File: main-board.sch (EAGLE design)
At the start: 53 parts, among them IC1 MEGA328-PB, IC2 MCP73831, IC3 LE33, Q1 3,6864 MHz, Q4 TSM2302CX, T1 IRF7306

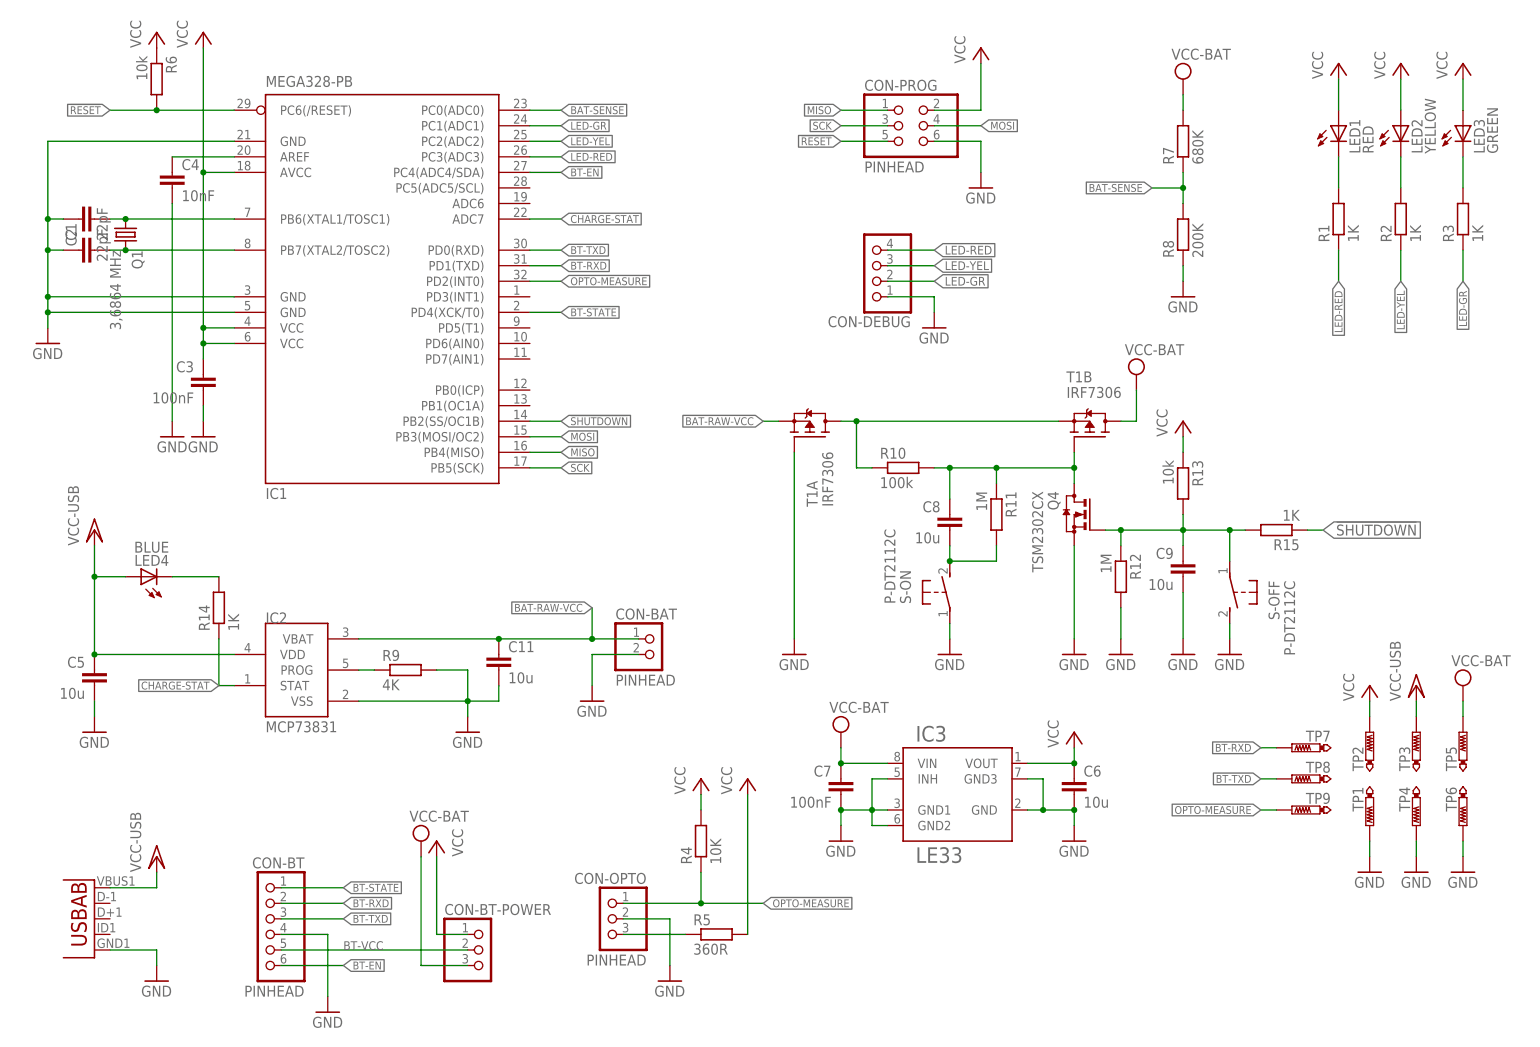
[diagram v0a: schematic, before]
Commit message: Optimize for BOM.
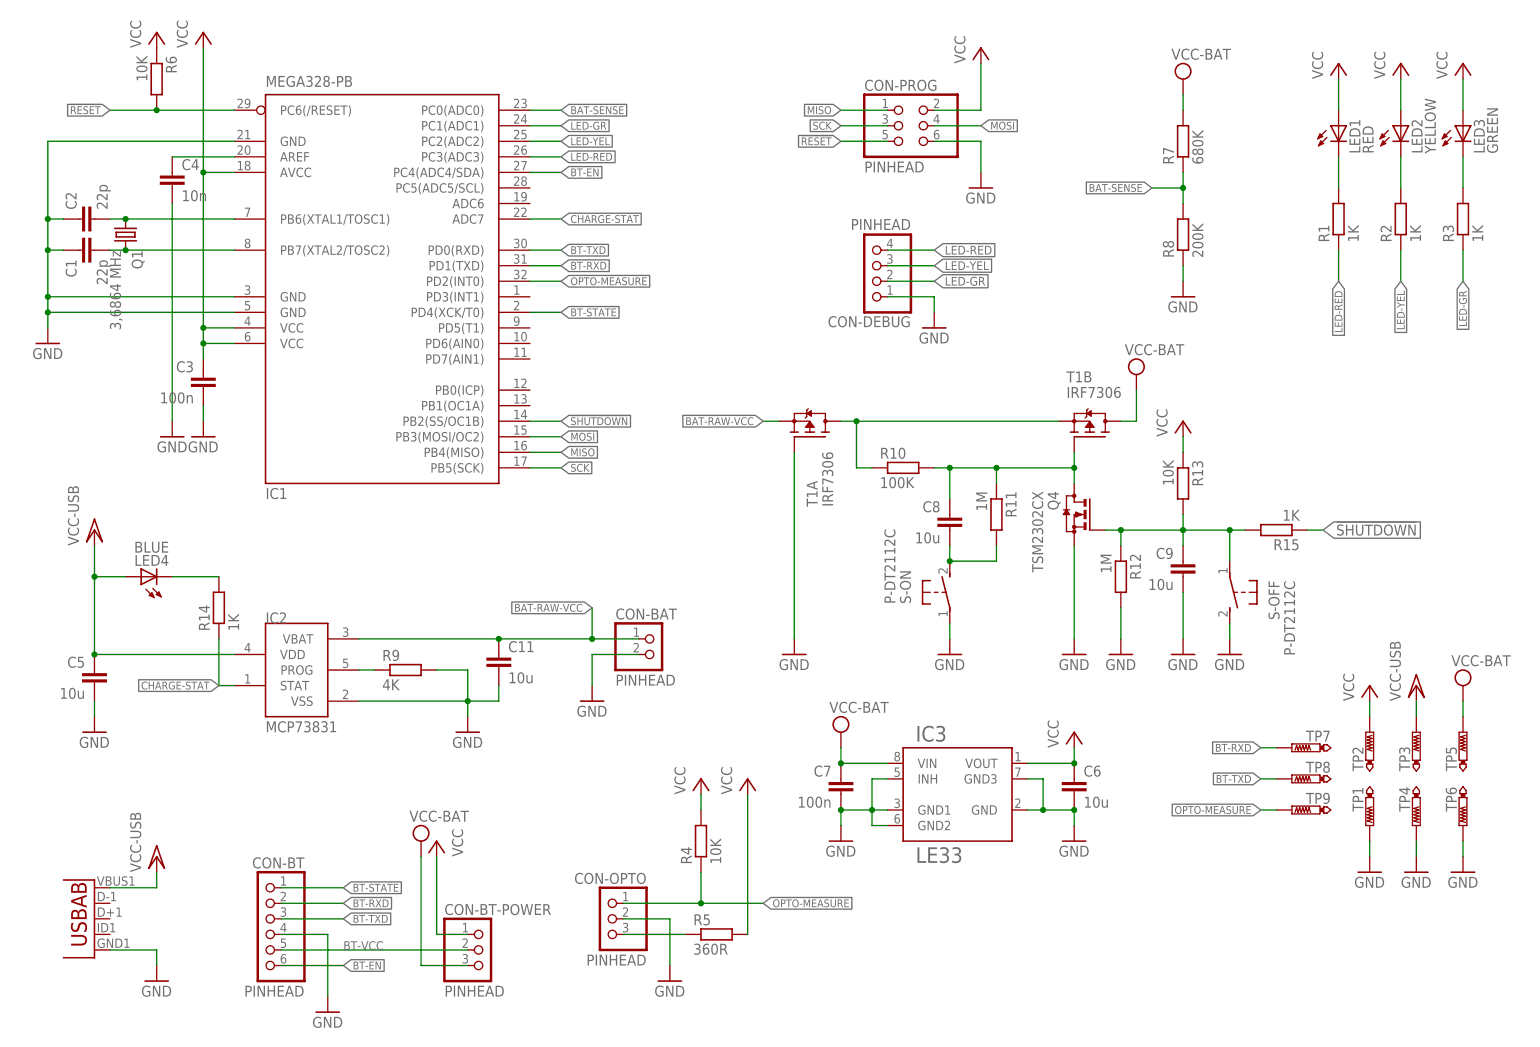
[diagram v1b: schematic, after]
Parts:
- C1, C2: value 22pF -> 22p
- C3, C7: value 100nF -> 100n
- C4: value 10nF -> 10n
- CON-BT-POWER, CON-DEBUG: value (none) -> PINHEAD
- R10: value 100k -> 100K
- R13, R6: value 10k -> 10K
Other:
- moved on the sheet: C1, C2
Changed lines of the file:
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@@
 <part name="Q1" library="crystal" deviceset="CRYSTAL" device="HC49UP" value="3,6864 MHz "/>
 <part name="IC1" library="atmel" deviceset="MEGA8" device="-AI" value="MEGA328-PB"/>
-<part name="C1" library="rcl" deviceset="C-EU" device="C0805" value="22pF"/>
-<part name="C2" library="rcl" deviceset="C-EU" device="C0805" value="22pF"/>
+<part name="C1" library="rcl" deviceset="C-EU" device="C0805" value="22p"/>
+<part name="C2" library="rcl" deviceset="C-EU" device="C0805" value="22p"/>
 <part name="GND1" library="supply1" deviceset="GND" device=""/>
 <part name="P+1" library="supply1" deviceset="VCC" device=""/>
-<part name="C3" library="rcl" deviceset="C-EU" device="C0805" value="100nF"/>
+<part name="C3" library="rcl" deviceset="C-EU" device="C0805" value="100n"/>
 <part name="GND2" library="supply1" deviceset="GND" device=""/>
 <part name="LED1" library="led" deviceset="LED" device="CHIP-LED0805" value="RED"/>
@@
 <part name="GND6" library="supply1" deviceset="GND" device=""/>
 <part name="P+7" library="supply1" deviceset="VCC" device=""/>
-<part name="R6" library="rcl" deviceset="R-EU_" device="R0805" value="10k"/>
+<part name="R6" library="rcl" deviceset="R-EU_" device="R0805" value="10K"/>
 <part name="P+8" library="supply1" deviceset="VCC" device=""/>
 <part name="R7" library="rcl" deviceset="R-EU_" device="R0805" value="680K"/>
@@
 <part name="SUPPLY1" library="supply2" deviceset="VCC" device="" value="VCC-BAT"/>
 <part name="GND7" library="supply1" deviceset="GND" device=""/>
-<part name="C4" library="rcl" deviceset="C-EU" device="C0805" value="10nF"/>
+<part name="C4" library="rcl" deviceset="C-EU" device="C0805" value="10n"/>
 <part name="GND8" library="supply1" deviceset="GND" device=""/>
 <part name="IC2" library="mcp73831" deviceset="MCP73831" device=""/>
@@
 <part name="TP9" library="testpad" deviceset="PTR1" device="B1,27" value="PTR1B1,27"/>
 <part name="IC3" library="v-reg-lowdrop" deviceset="LE33" device=""/>
-<part name="C7" library="rcl" deviceset="C-EU" device="C0805" value="100nF"/>
+<part name="C7" library="rcl" deviceset="C-EU" device="C0805" value="100n"/>
 <part name="GND15" library="supply1" deviceset="GND" device=""/>
 <part name="SUPPLY3" library="supply2" deviceset="VCC" device="" value="VCC-BAT"/>
@@
 <part name="C8" library="rcl" deviceset="C-EU" device="C0805" value="10u"/>
 <part name="R12" library="rcl" deviceset="R-EU_" device="R0805" value="1M"/>
-<part name="R13" library="rcl" deviceset="R-EU_" device="R0805" value="10k"/>
+<part name="R13" library="rcl" deviceset="R-EU_" device="R0805" value="10K"/>
 <part name="C9" library="rcl" deviceset="C-EU" device="C0805" value="10u"/>
-<part name="R10" library="rcl" deviceset="R-EU_" device="R0805" value="100k"/>
+<part name="R10" library="rcl" deviceset="R-EU_" device="R0805" value="100K"/>
 <part name="Q4" library="transistor-small-signal" deviceset="BSS123" device="" value="TSM2302CX"/>
 <part name="GND48" library="supply1" library_urn="urn:adsk.eagle:library:371" deviceset="GND" device=""/>
@@
 <part name="C5" library="rcl" deviceset="C-EU" device="C0805" value="10u"/>
 <part name="C6" library="rcl" deviceset="C-EU" device="C0805" value="10u"/>
-<part name="CON-DEBUG" library="pinhead" deviceset="PINHD-1X4" device=""/>
+<part name="CON-DEBUG" library="pinhead" deviceset="PINHD-1X4" device="" value="PINHEAD"/>
 <part name="GND17" library="supply1" deviceset="GND" device=""/>
 <part name="T1" library="transistor-fet" deviceset="IRF7306" device=""/>
 <part name="GND18" library="supply1" library_urn="urn:adsk.eagle:library:371" deviceset="GND" device=""/>
 <part name="P+13" library="supply1" deviceset="VCC" device=""/>
-<part name="CON-BT-POWER" library="pinhead" deviceset="PINHD-1X3" device=""/>
+<part name="CON-BT-POWER" library="pinhead" deviceset="PINHD-1X3" device="" value="PINHEAD"/>
 <part name="P+14" library="supply1" deviceset="VCC" device=""/>
 <part name="S-ON" library="switch-tact" deviceset="DTSM-3" device="" value="P-DT2112C"/>
@@
 <instance part="Q1" gate="G$1" x="25.4" y="137.16" rot="R270"/>
 <instance part="IC1" gate="G$1" x="66.04" y="132.08"/>
-<instance part="C1" gate="G$1" x="17.78" y="134.62" rot="R90"/>
-<instance part="C2" gate="G$1" x="17.78" y="139.7" rot="MR270"/>
+<instance part="C1" gate="G$1" x="17.78" y="134.62" rot="MR270"/>
+<instance part="C2" gate="G$1" x="17.78" y="139.7" rot="R90"/>
 <instance part="GND1" gate="1" x="12.7" y="119.38"/>
 <instance part="P+1" gate="VCC" x="38.1" y="170.18"/>

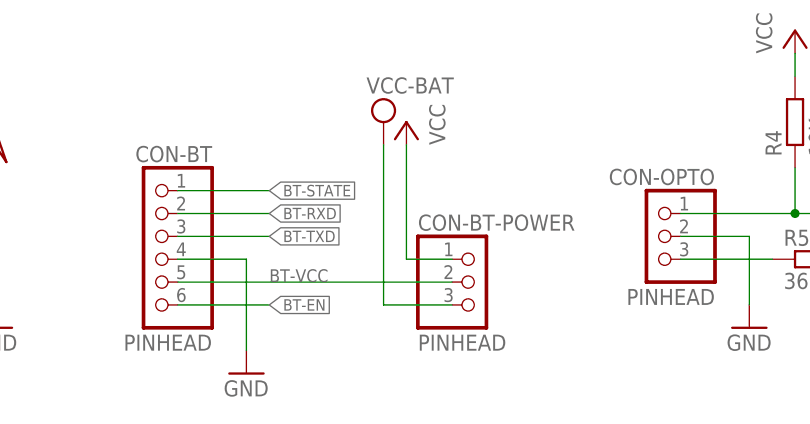
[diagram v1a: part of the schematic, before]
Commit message: Con-bt-power -> jumper BT power.
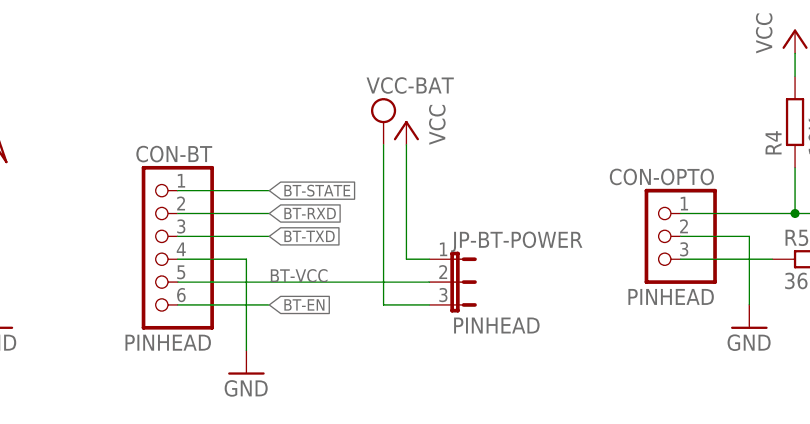
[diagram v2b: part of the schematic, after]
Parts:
- removed CON-BT-POWER: PINHEAD, pinhead:PINHD-1X3
- added JP-BT-POWER: PINHEAD, jumper:JP2E
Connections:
- net BT-VCC: now also JP-BT-POWER.2; no longer CON-BT-POWER.2
- net VCC: now also JP-BT-POWER.1; no longer CON-BT-POWER.1
- net VCC-BAT: now also JP-BT-POWER.3; no longer CON-BT-POWER.3
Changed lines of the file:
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@@
 <part name="GND18" library="supply1" library_urn="urn:adsk.eagle:library:371" deviceset="GND" device=""/>
 <part name="P+13" library="supply1" deviceset="VCC" device=""/>
-<part name="CON-BT-POWER" library="pinhead" deviceset="PINHD-1X3" device="" value="PINHEAD"/>
+<part name="JP-BT-POWER" library="jumper" deviceset="JP2E" device="" value="PINHEAD"/>
 <part name="P+14" library="supply1" deviceset="VCC" device=""/>
 <part name="S-ON" library="switch-tact" deviceset="DTSM-3" device="" value="P-DT2112C"/>
@@
 <instance part="GND18" gate="1" x="134.62" y="68.58"/>
 <instance part="P+13" gate="VCC" x="127" y="48.26"/>
-<instance part="CON-BT-POWER" gate="A" x="83.82" y="20.32"/>
+<instance part="JP-BT-POWER" gate="1" x="81.28" y="20.32" rot="R270"/>
 <instance part="P+14" gate="VCC" x="76.2" y="38.1" rot="MR0"/>
 <instance part="S-ON" gate="G$1" x="160.02" y="78.74" smashed="yes">
@@
 <pinref part="P+14" gate="VCC" pin="VCC"/>
 <wire x1="76.2" y1="35.56" x2="76.2" y2="22.86" width="0.1524" layer="91"/>
-<pinref part="CON-BT-POWER" gate="A" pin="1"/>
-<wire x1="76.2" y1="22.86" x2="81.28" y2="22.86" width="0.1524" layer="91"/>
+<pinref part="JP-BT-POWER" gate="1" pin="1"/>
+<wire x1="76.2" y1="22.86" x2="78.74" y2="22.86" width="0.1524" layer="91"/>
 </segment>
 </net>
@@
 <segment>
 <pinref part="CON-BT" gate="A" pin="5"/>
-<pinref part="CON-BT-POWER" gate="A" pin="2"/>
-<wire x1="50.8" y1="20.32" x2="81.28" y2="20.32" width="0.1524" layer="91"/>
+<pinref part="JP-BT-POWER" gate="1" pin="2"/>
+<wire x1="50.8" y1="20.32" x2="78.74" y2="20.32" width="0.1524" layer="91"/>
 <label x="60.96" y="20.32" size="1.4224" layer="95"/>
 </segment>
@@
 </segment>
 <segment>
-<pinref part="CON-BT-POWER" gate="A" pin="3"/>
-<wire x1="81.28" y1="17.78" x2="73.66" y2="17.78" width="0.1524" layer="91"/>
+<pinref part="JP-BT-POWER" gate="1" pin="3"/>
+<wire x1="78.74" y1="17.78" x2="73.66" y2="17.78" width="0.1524" layer="91"/>
 <wire x1="73.66" y1="17.78" x2="73.66" y2="35.56" width="0.1524" layer="91"/>
 <pinref part="SUPPLY4" gate="G$1" pin="VCC"/>

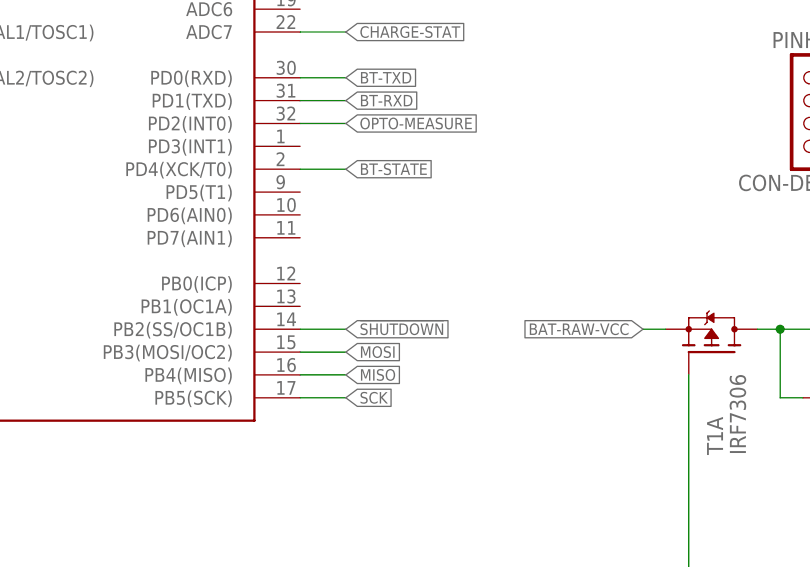
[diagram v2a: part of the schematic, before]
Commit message: Connect OPTO-MEASURE to ICP (PB0).
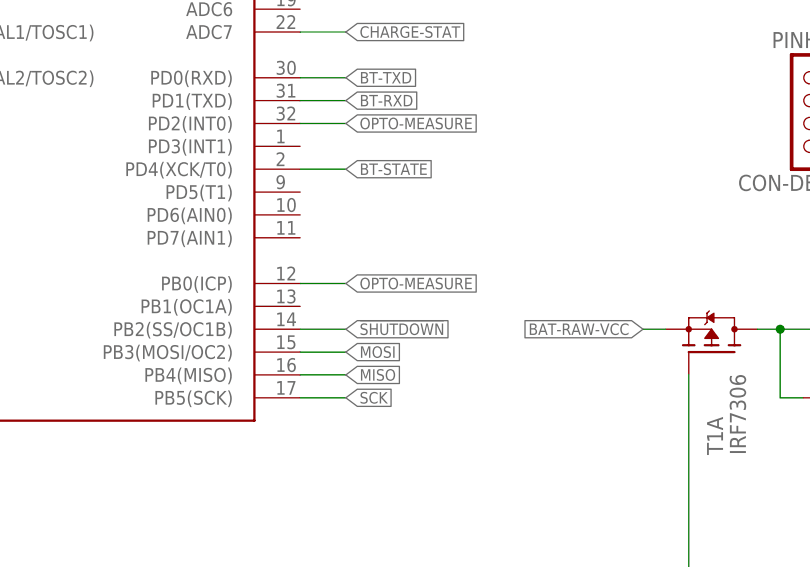
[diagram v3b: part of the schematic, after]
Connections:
- net OPTO-MEASURE: now also IC1.PB0(ICP)
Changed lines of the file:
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@@
 <label x="96.52" y="129.54" size="1.27" layer="95" xref="yes"/>
+</segment>
+<segment>
+<pinref part="IC1" gate="G$1" pin="PB0(ICP)"/>
+<wire x1="96.52" y1="111.76" x2="91.44" y2="111.76" width="0.1524" layer="91"/>
+<label x="96.52" y="111.76" size="1.27" layer="95" xref="yes"/>
 </segment>
 </net>

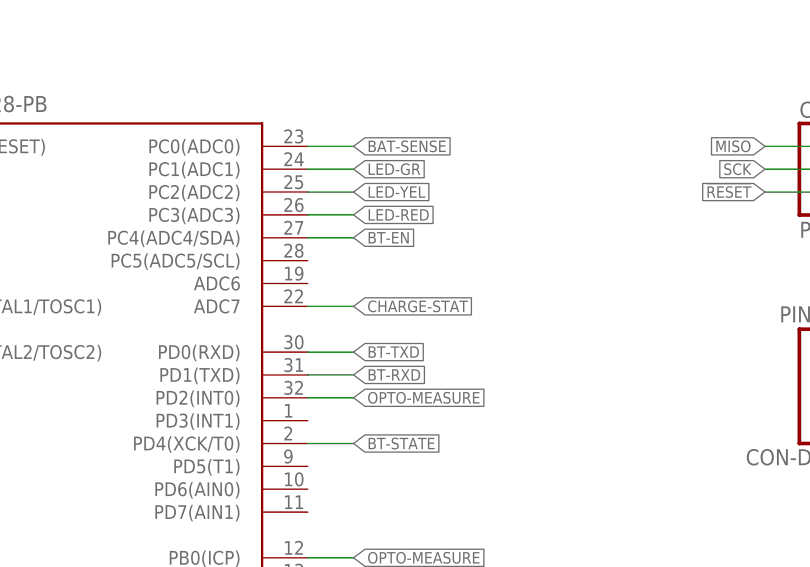
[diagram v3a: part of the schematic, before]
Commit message: Move CHARGE-STAT to digital pin.
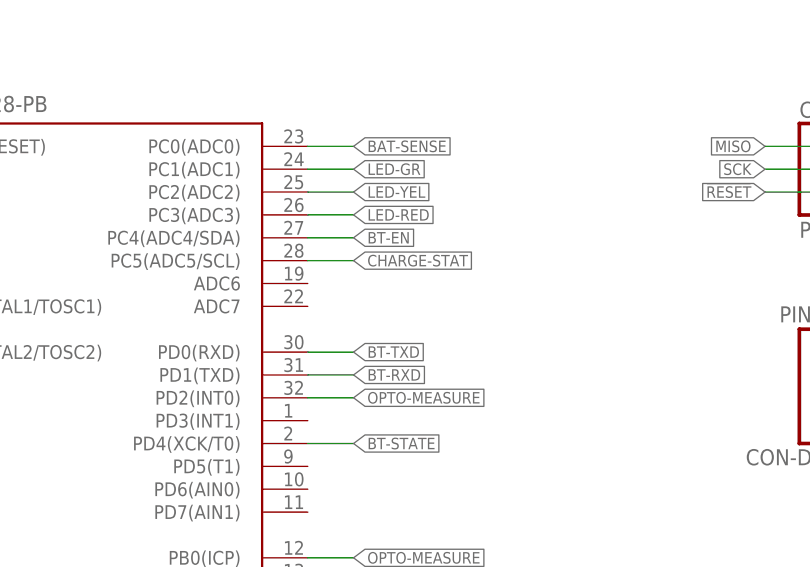
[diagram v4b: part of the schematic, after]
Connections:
- net CHARGE-STAT: now also IC1.PC5(ADC5/SCL); no longer IC1.ADC7
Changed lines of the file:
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@@
 </segment>
 <segment>
-<pinref part="IC1" gate="G$1" pin="ADC7"/>
-<wire x1="91.44" y1="139.7" x2="96.52" y2="139.7" width="0.1524" layer="91"/>
-<label x="96.52" y="139.7" size="1.27" layer="95" xref="yes"/>
+<label x="96.52" y="144.78" size="1.27" layer="95" xref="yes"/>
+<pinref part="IC1" gate="G$1" pin="PC5(ADC5/SCL)"/>
+<wire x1="96.52" y1="144.78" x2="91.44" y2="144.78" width="0.1524" layer="91"/>
 </segment>
 </net>
